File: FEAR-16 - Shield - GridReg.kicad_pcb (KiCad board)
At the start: 4 copper layers, 67.3 x 39.2 mm, 65 parts, among them J1 Channel-In, J101 Supply, J102 Signals, J103 Channel-In, Q201 NDFPD1N150CG, U201 OPA2156xD, U202 OPA2156xD, U203 OPA2156xD, U204 OPA2156xD

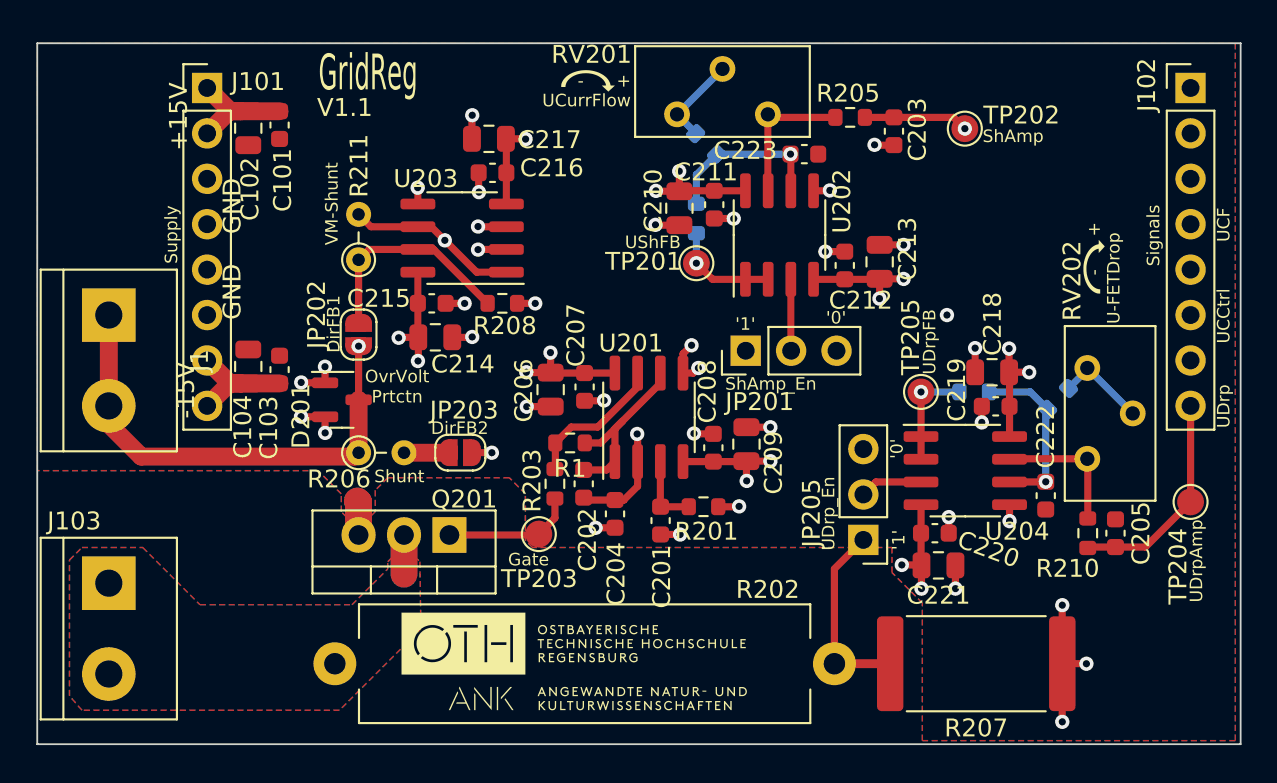
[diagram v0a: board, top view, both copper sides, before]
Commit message: Added option to invert FET-Gate voltage
Added JP206 (3Pad Solder Jumper) and JP204 (2Pad Solder Jumper)
These using the, until now, unused second OpAmp of U201.

--> Jumpers that allow to invert the FET-Gate Voltage

FET-Gate Voltage acts as Grid-Regulation (inverting):
- Close JP206 Pins 2 with 3
- Close JP204
- Use R215 = 1Meg

FET-Gate Voltage acts as Cath-Regulation (non inverting):
- Close JP206 Pins 2 with 1
- Open  JP204
- Use R215 = 0R (Short-Circuit)

Candidate for V1.2
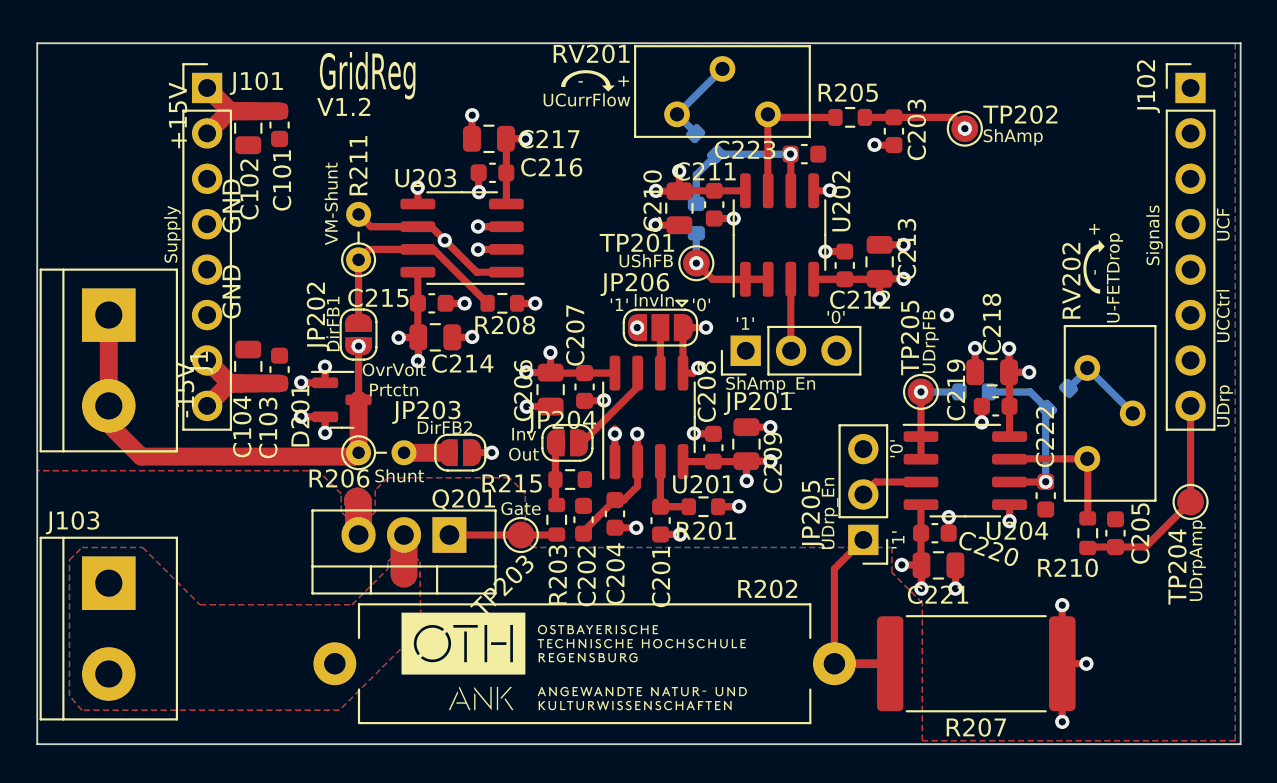
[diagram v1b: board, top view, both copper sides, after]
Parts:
- added JP204: Invert_{Out}, Jumper:SolderJumper-2_P1.3mm_Open_RoundedPad1.0x1.5mm, F.Cu at (22.6, 22.4)
- added JP206: Invert_{In}, Jumper:SolderJumper-3_P1.3mm_Open_RoundedPad1.0x1.5mm, F.Cu at (27.9, 15.9)
- moved R215 2.05 mm to (22.8, 24.4)
- moved R203 2.01 mm to (22.1, 26.6)
- moved C202 2.01 mm to (23.6, 26.6)
- moved TP203 1.00 mm to (20.1, 27.5)
- renumbered R1 to R215
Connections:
- C202 pad 2: Net-(U201B--) -> Net-(JP206-B)
- R203 pad 1: Net-(R1-Pad2) -> Net-(JP204-A)
- R215 pad 1: Net-(U201B--) -> Net-(JP206-B)
- R215 pad 2: Net-(R1-Pad2) -> Net-(JP204-A)
- U201 pad 1: Net-(U201B--) -> Net-(JP206-B)
- U201 pad 6: Net-(U201B--) -> Net-(JP206-C)
- U201 pad 7: Net-(R1-Pad2) -> Net-(JP204-B)
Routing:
- net Net-(U201B--): track 10.5 -> 0.00 mm
- net Net-(JP206-B): track 0.00 -> 8.30 mm, vias 0 -> 2
- net Net-(R1-Pad2): track 8.15 -> 0.00 mm
- net Net-(JP204-B): track 0.00 -> 5.35 mm
- net Net-(JP204-A): track 0.00 -> 3.63 mm
- net Net-(JP206-C): track 0.00 -> 3.12 mm
- net GND: track 42.4 -> 44.6 mm
- net Net-(Q201-G): track 7.38 -> 6.01 mm
- net /Channel/USh: track 25.0 -> 25.8 mm
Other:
- board text added: "'0'"
- board text added: "'1'"
- board text added: "Inv Out"
- board text added: "InvIn"
- board text added: "V1.2"
- board text removed: "V1.1"
